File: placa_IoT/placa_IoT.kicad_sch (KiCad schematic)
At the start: 0 parts

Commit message: Esquemático add
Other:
- added sheet ALIMENTACION (alimentacion.kicad_sch)
- added sheet BATERIA (bateria.kicad_sch)
- added sheet MICROCONTROLADOR (,icrocontrolador.kicad_sch)
- added sheet RF (RF.kicad_sch)
- company: (none) -> ELE0226CL
- title: (none) -> Bloque Batería
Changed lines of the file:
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@@
 	(generator "eeschema")
 	(generator_version "10.0")
-	(paper "A4")
+	(paper "A3")
+	(title_block
+		(title "Bloque Batería")
+		(date "2026-05-19")
+		(company "ELE0226CL")
+		(comment 1 "Lara DM")
+	)
+	(sheet
+		(at 167.64 73.66)
+		(size 90.17 152.4)
+		(exclude_from_sim no)
+		(in_bom yes)
+		(on_board yes)
+		(dnp no)
+		(fields_autoplaced yes)
+		(stroke
+			(width 0.1524)
+			(type solid)
+		)
+		(fill
+			(color 0 0 0 0)
+		)
+		(property "Sheetname" "MICROCONTROLADOR"
+			(at 167.64 72.9484 0)
+			(show_name no)
+			(do_not_autoplace no)
+			(effects
+				(font
+					(size 1.27 1.27)
+				)
+				(justify left bottom)
+			)
+		)
+		(property "Sheetfile" ",icrocontrolador.kicad_sch"
+			(at 167.64 226.6446 0)
+			(show_name no)
+			(do_not_autoplace no)
+			(effects
+				(font
+					(size 1.27 1.27)
+				)
+				(justify left top)
+			)
+		)
+		(instances
+			(project "placa_IoT"
+				(path "/5cf00a4a-c4d0-4d7e-b436-de913efc1992"
+					(page "3")
+				)
+			)
+		)
+	)
+	(sheet
+		(at 31.75 36.83)
+		(size 96.52 100.33)
+		(exclude_from_sim no)
+		(in_bom yes)
+		(on_board yes)
+		(dnp no)
+		(fields_autoplaced yes)
+		(stroke
+			(width 0.1524)
+			(type solid)
+		)
+		(fill
+			(color 0 0 0 0)
+		)
+		(property "Sheetname" "RF"
+			(at 31.75 36.1184 0)
+			(show_name no)
+			(do_not_autoplace no)
+			(effects
+				(font
+					(size 1.27 1.27)
+				)
+				(justify left bottom)
+			)
+		)
+		(property "Sheetfile" "RF.kicad_sch"
+			(at 31.75 137.7446 0)
+			(show_name no)
+			(do_not_autoplace no)
+			(effects
+				(font
+					(size 1.27 1.27)
+				)
+				(justify left top)
+			)
+		)
+		(instances
+			(project "placa_IoT"
+				(path "/5cf00a4a-c4d0-4d7e-b436-de913efc1992"
+					(page "5")
+				)
+			)
+		)
+	)
+	(sheet
+		(at 30.48 180.34)
+		(size 101.6 83.82)
+		(exclude_from_sim no)
+		(in_bom yes)
+		(on_board yes)
+		(dnp no)
+		(fields_autoplaced yes)
+		(stroke
+			(width 0.1524)
+			(type solid)
+		)
+		(fill
+			(color 0 0 0 0)
+		)
+		(property "Sheetname" "BATERIA"
+			(at 30.48 179.6284 0)
+			(show_name no)
+			(do_not_autoplace no)
+			(effects
+				(font
+					(size 1.27 1.27)
+				)
+				(justify left bottom)
+			)
+		)
+		(property "Sheetfile" "bateria.kicad_sch"
+			(at 30.48 264.7446 0)
+			(show_name no)
+			(do_not_autoplace no)
+			(effects
+				(font
+					(size 1.27 1.27)
+				)
+				(justify left top)
+			)
+		)
+		(instances
+			(project "placa_IoT"
+				(path "/5cf00a4a-c4d0-4d7e-b436-de913efc1992"
+					(page "4")
+				)
+			)
+		)
+	)
+	(sheet
+		(at 290.83 85.09)
+		(size 102.87 127)
+		(exclude_from_sim no)
+		(in_bom yes)
+		(on_board yes)
+		(dnp no)
+		(fields_autoplaced yes)
+		(stroke
+			(width 0.1524)
+			(type solid)
+		)
+		(fill
+			(color 0 0 0 0)
+		)
+		(property "Sheetname" "ALIMENTACION"
+			(at 290.83 84.3784 0)
+			(show_name no)
+			(do_not_autoplace no)
+			(effects
+				(font
+					(size 1.27 1.27)
+				)
+				(justify left bottom)
+			)
+		)
+		(property "Sheetfile" "alimentacion.kicad_sch"
+			(at 290.83 212.6746 0)
+			(show_name no)
+			(do_not_autoplace no)
+			(effects
+				(font
+					(size 1.27 1.27)
+				)
+				(justify left top)
+			)
+		)
+		(instances
+			(project "placa_IoT"
+				(path "/5cf00a4a-c4d0-4d7e-b436-de913efc1992"
+					(page "2")
+				)
+			)
+		)
+	)
 	(sheet_instances
 		(path "/"

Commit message: USB completed
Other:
- added sheet USB (USB.kicad_sch)
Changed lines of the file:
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@@
 	)
 	(sheet
-		(at 167.64 73.66)
-		(size 90.17 152.4)
+		(at 157.48 25.4)
+		(size 119.38 234.95)
 		(exclude_from_sim no)
 		(in_bom yes)
@@
 		)
 		(property "Sheetname" "MICROCONTROLADOR"
-			(at 167.64 72.9484 0)
+			(at 157.48 24.6884 0)
 			(show_name no)
 			(do_not_autoplace no)
@@
 		)
 		(property "Sheetfile" ",icrocontrolador.kicad_sch"
-			(at 167.64 226.6446 0)
+			(at 157.48 260.9346 0)
 			(show_name no)
 			(do_not_autoplace no)
@@
 	)
 	(sheet
-		(at 31.75 36.83)
-		(size 96.52 100.33)
+		(at 31.75 25.4)
+		(size 114.3 123.19)
 		(exclude_from_sim no)
 		(in_bom yes)
@@
 		)
 		(property "Sheetname" "RF"
-			(at 31.75 36.1184 0)
+			(at 31.75 24.6884 0)
 			(show_name no)
 			(do_not_autoplace no)
@@
 		)
 		(property "Sheetfile" "RF.kicad_sch"
-			(at 31.75 137.7446 0)
+			(at 31.75 149.1746 0)
 			(show_name no)
 			(do_not_autoplace no)
@@
 	)
 	(sheet
-		(at 30.48 180.34)
-		(size 101.6 83.82)
+		(at 30.48 168.91)
+		(size 115.57 95.25)
 		(exclude_from_sim no)
 		(in_bom yes)
@@
 		)
 		(property "Sheetname" "BATERIA"
-			(at 30.48 179.6284 0)
+			(at 30.48 168.1984 0)
 			(show_name no)
 			(do_not_autoplace no)
@@
 	)
 	(sheet
-		(at 290.83 85.09)
-		(size 102.87 127)
+		(at 288.29 16.51)
+		(size 115.57 93.98)
+		(exclude_from_sim no)
+		(in_bom yes)
+		(on_board yes)
+		(dnp no)
+		(fields_autoplaced yes)
+		(stroke
+			(width 0.1524)
+			(type solid)
+		)
+		(fill
+			(color 0 0 0 0)
+		)
+		(property "Sheetname" "USB"
+			(at 288.29 15.7984 0)
+			(show_name no)
+			(do_not_autoplace no)
+			(effects
+				(font
+					(size 1.27 1.27)
+				)
+				(justify left bottom)
+			)
+		)
+		(property "Sheetfile" "USB.kicad_sch"
+			(at 288.29 111.0746 0)
+			(show_name no)
+			(do_not_autoplace no)
+			(effects
+				(font
+					(size 1.27 1.27)
+				)
+				(justify left top)
+			)
+		)
+		(instances
+			(project "placa_IoT"
+				(path "/5cf00a4a-c4d0-4d7e-b436-de913efc1992"
+					(page "6")
+				)
+			)
+		)
+	)
+	(sheet
+		(at 288.29 119.38)
+		(size 114.3 127)
 		(exclude_from_sim no)
 		(in_bom yes)
@@
 		)
 		(property "Sheetname" "ALIMENTACION"
-			(at 290.83 84.3784 0)
+			(at 288.29 118.6684 0)
 			(show_name no)
 			(do_not_autoplace no)
@@
 		)
 		(property "Sheetfile" "alimentacion.kicad_sch"
-			(at 290.83 212.6746 0)
-			(show_name no)
-			(do_not_autoplace no)
+			(at 288.29 246.9646 0)
+			(show_name no)
+			(do_not_autoplace no)

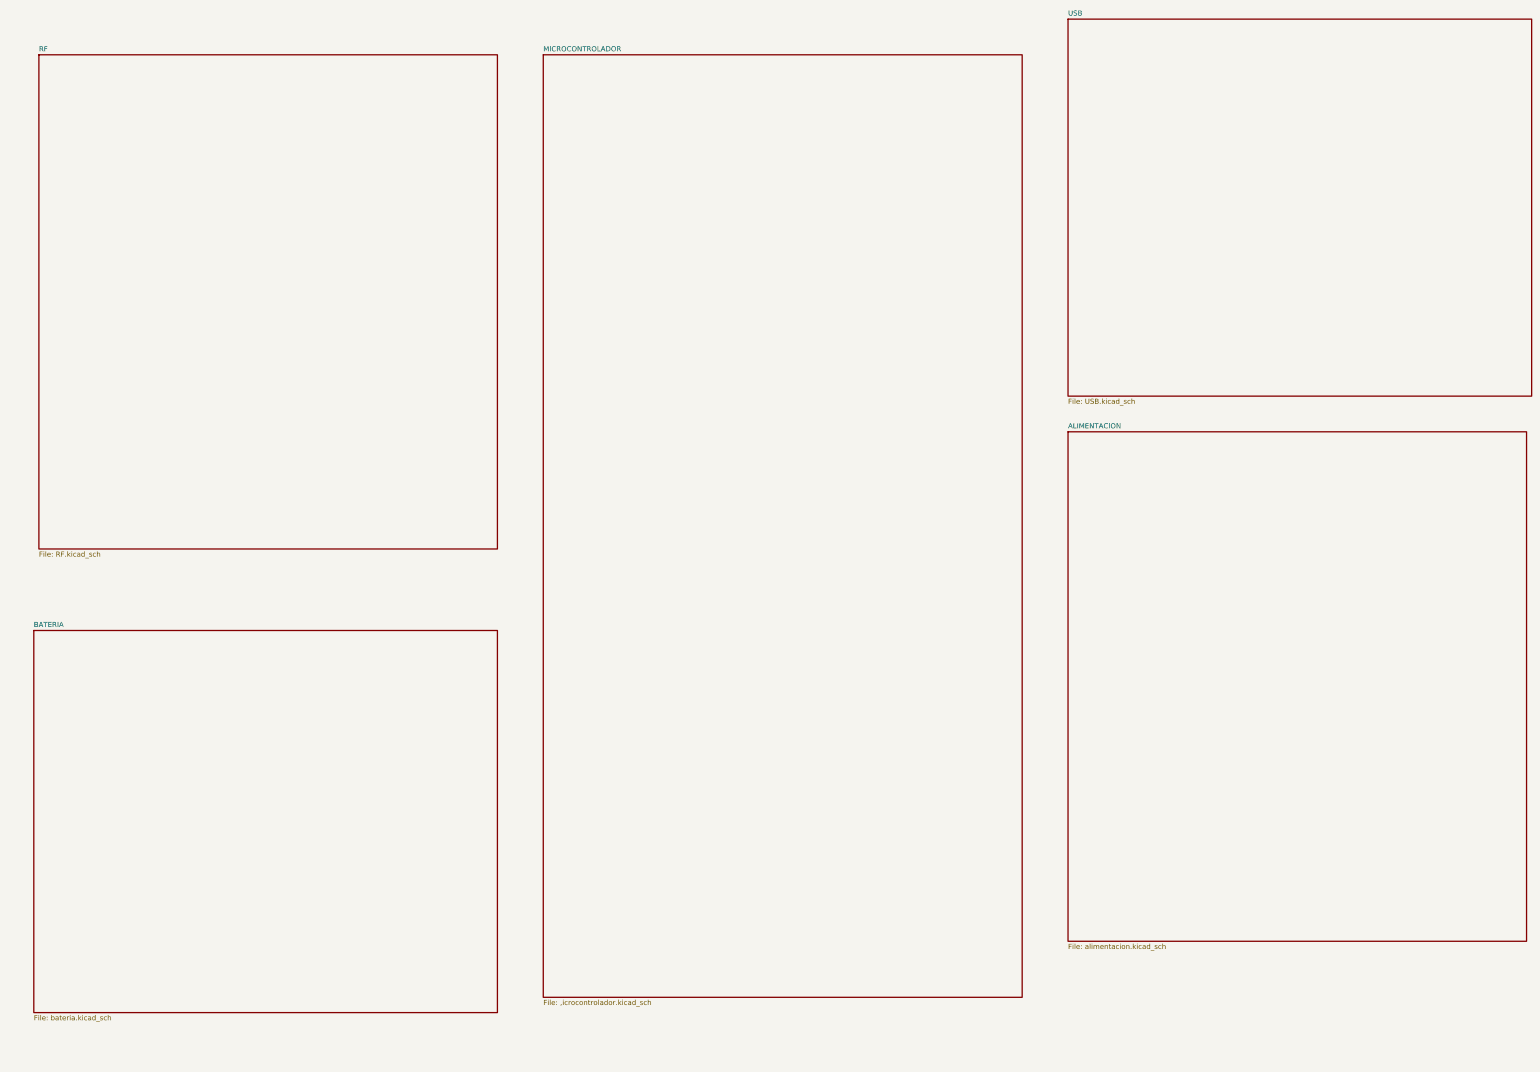
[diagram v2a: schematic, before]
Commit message: Falta unir pines
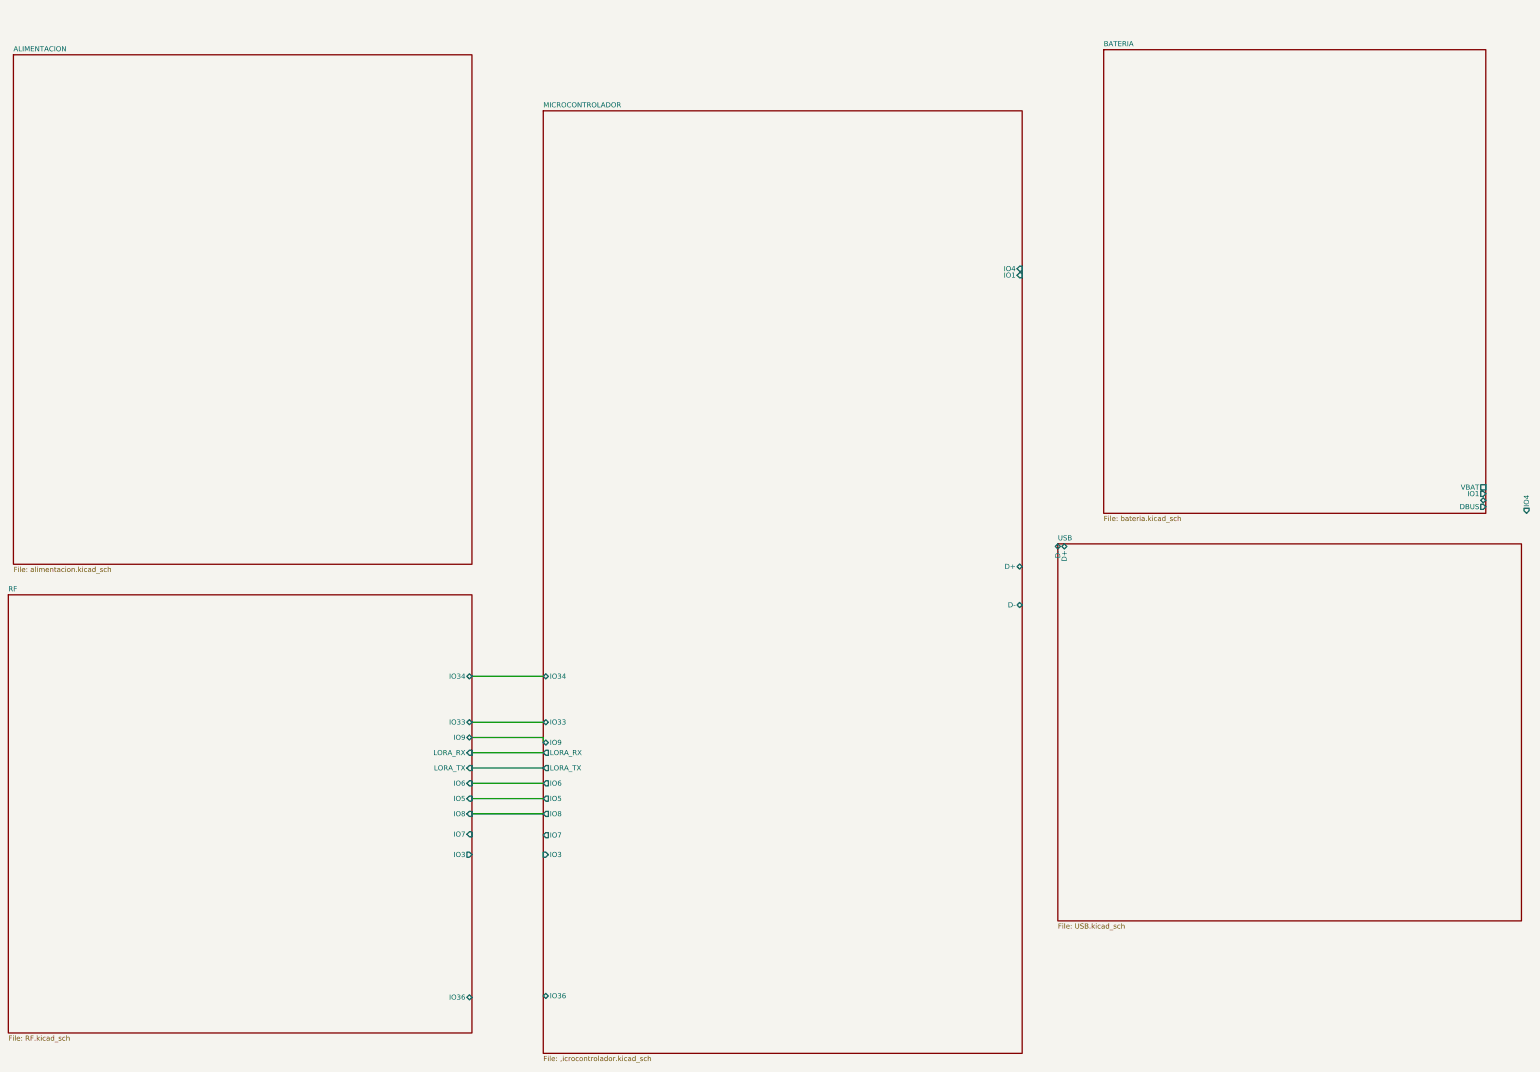
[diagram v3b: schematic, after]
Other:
- sheet BATERIA ports: added , DBUS, IO1, IO4, VBAT; removed none
- sheet MICROCONTROLADOR ports: added D+, D-, IO1, IO3, IO33, IO34, IO36, IO4, IO5, IO6, IO7, IO8, IO9, LORA_RX, LORA_TX; removed none
- sheet RF ports: added IO3, IO33, IO34, IO36, IO5, IO6, IO7, IO8, IO9, LORA_RX, LORA_TX; removed none
- sheet USB ports: added D+, D-; removed none
